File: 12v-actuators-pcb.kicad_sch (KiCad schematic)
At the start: 11 parts, among them J1 12V IN, J2 12V OUT, J3 12V OUT, J4 12V OUT, Q1 SUM110P06-08L, U1 NUCLEO-F042K6, X1 ESC_Emax_Bullet_15A, X2 ESC_Emax_Bullet_15A, X3 ESC_Emax_Bullet_15A, X4 ESC_Emax_Bullet_35A, X5 ESC_Emax_Bullet_35A

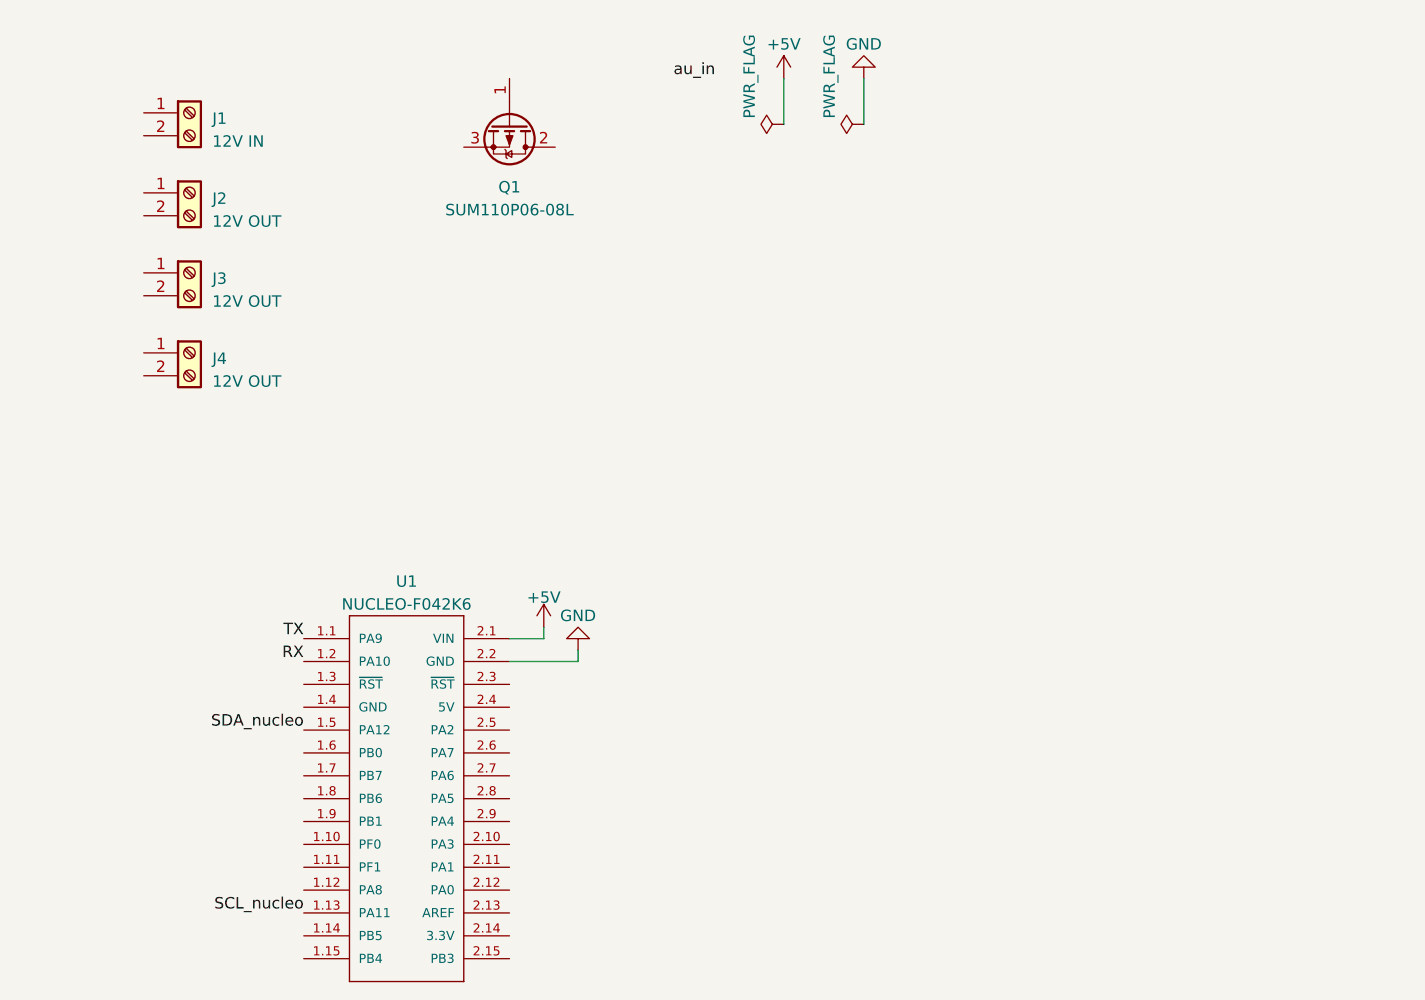
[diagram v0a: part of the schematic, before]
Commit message: WIP: Arrêt d'urgence
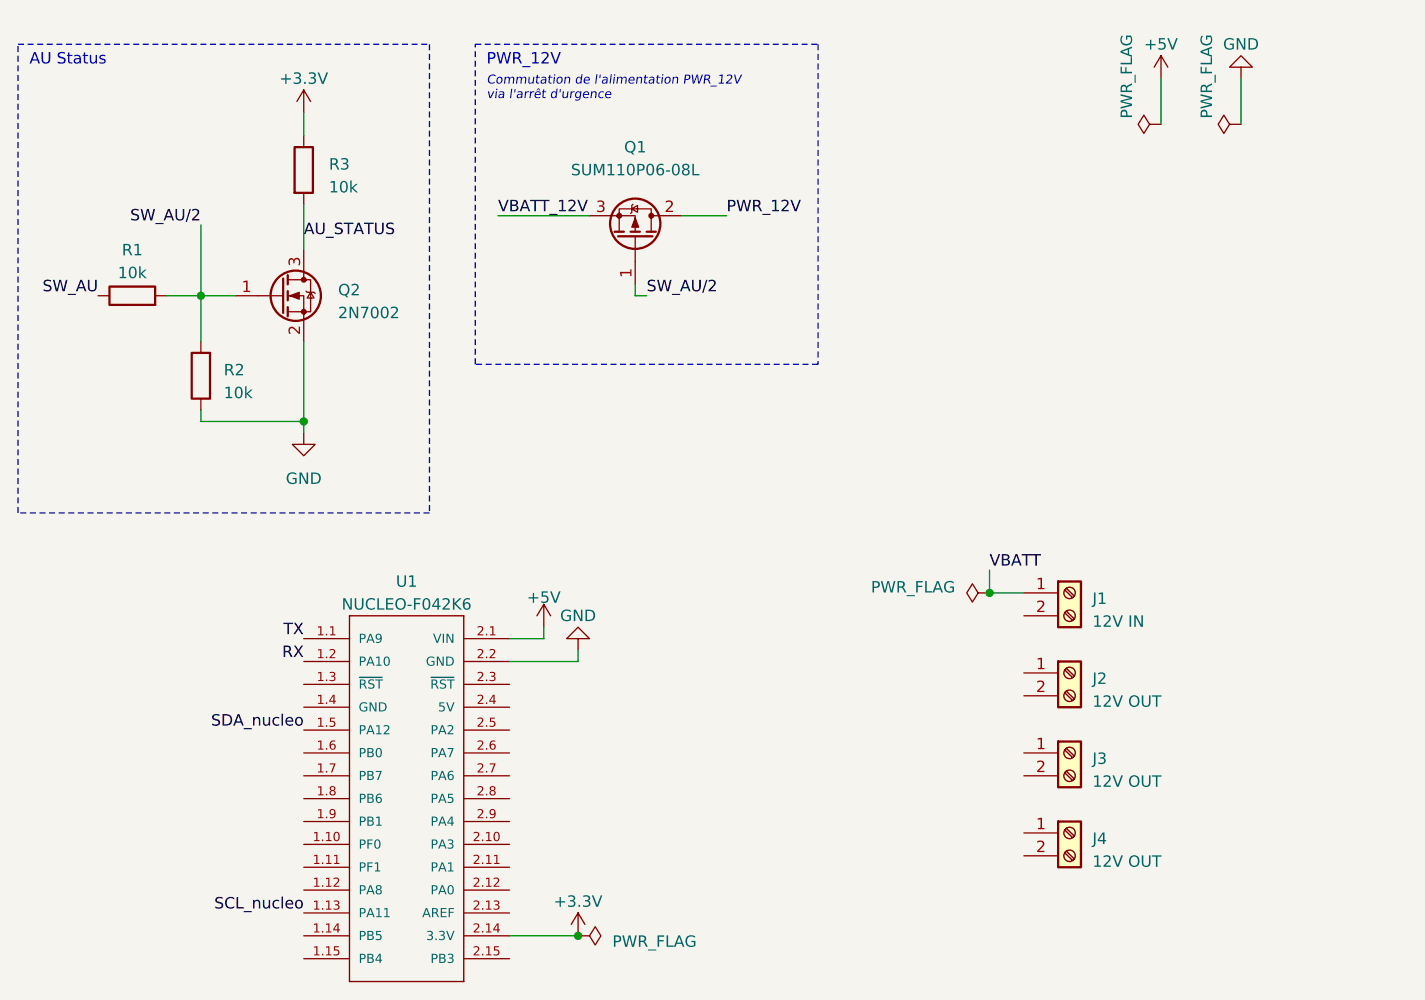
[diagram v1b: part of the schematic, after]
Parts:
- added Q2: 2N7002, Package_TO_SOT_SMD:SOT-23, symbol Transistor_FET:2N7002
- added R1, R2, R3: 10k, Resistor_SMD:R_0201_0603Metric, symbol Device:R
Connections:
- net GND: now also Q2.2 (S), R2.1
- net SW_AU/2: now reaches Q1.1 (G)
- net SW_AU/2: now also Q2.1 (G), R1.2, R2.2
- net PWR_12V: now reaches Q1.2 (D)
- net VBATT_12V: now reaches Q1.3 (S)
- net VBATT: now reaches J1.1 (Pin_1)
- net +3.3V: now reaches U1.2.14 (3.3V)
- net +3.3V: now also R3.1
- new net AU_STATUS: Q2.3 (D), R3.2
- new net SW_AU: R1.1
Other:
- note added: "AU Status"
- note added: "Commutation de l'alimentation PWR_12V via l'arrêt d'urgence"
- note added: "PWR_12V"
- moved on the sheet: J1, J2, J3, J4, Q1

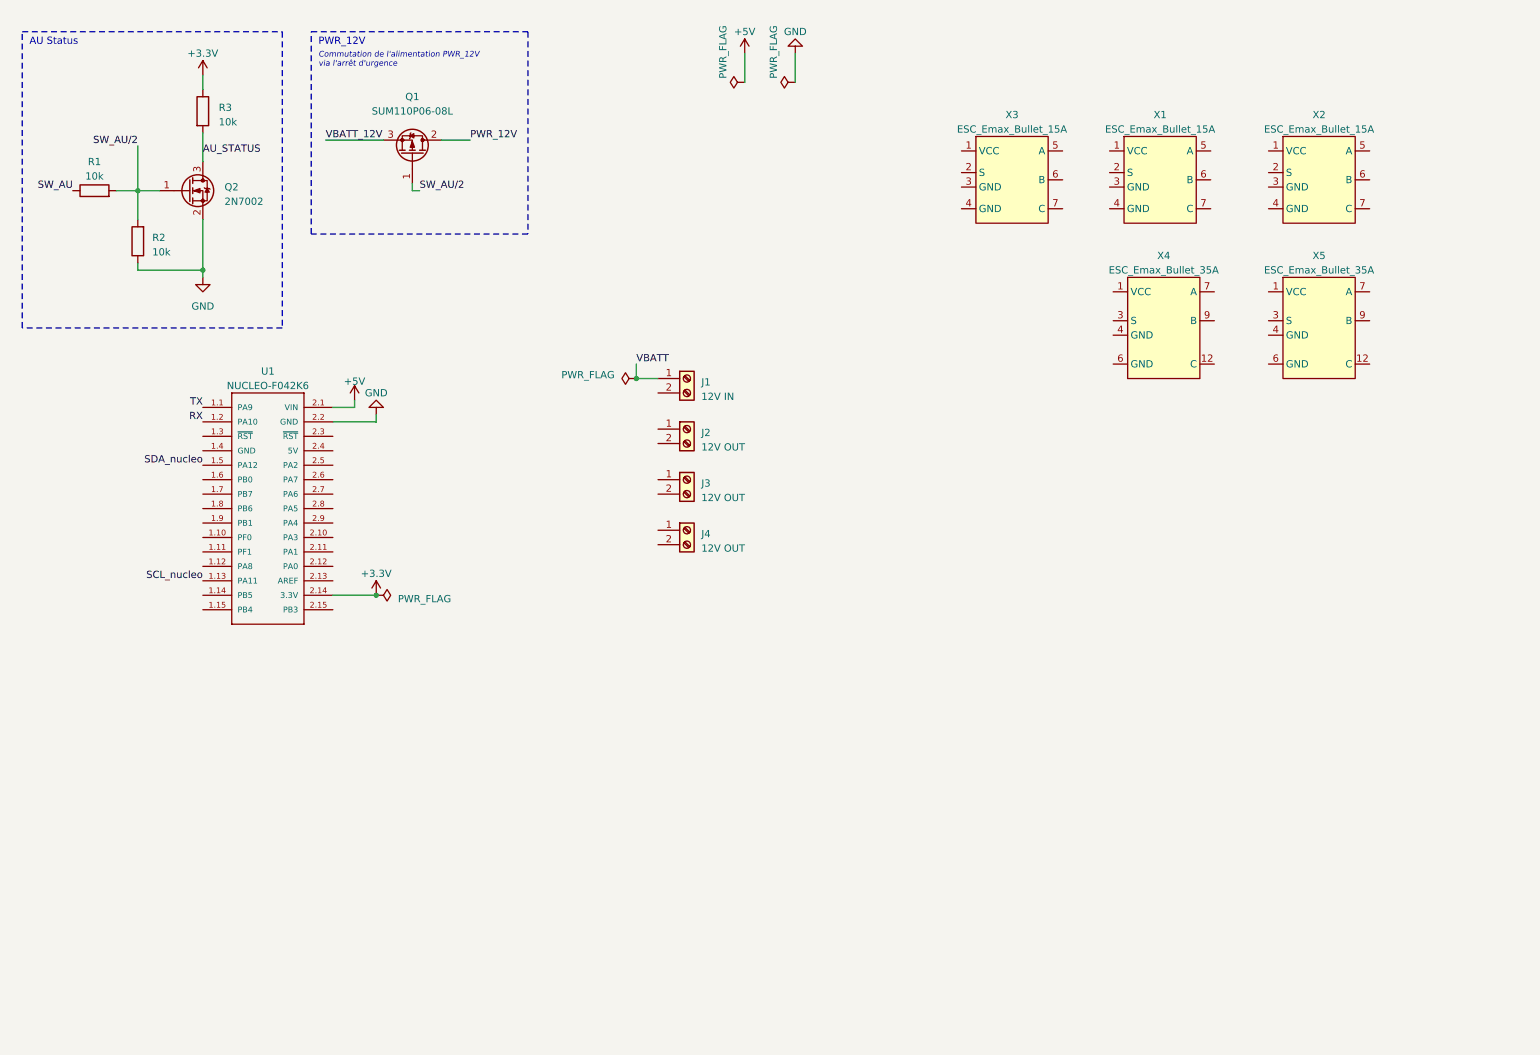
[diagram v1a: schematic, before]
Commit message: Schéma AU fait + ESC + électrovannes débuté
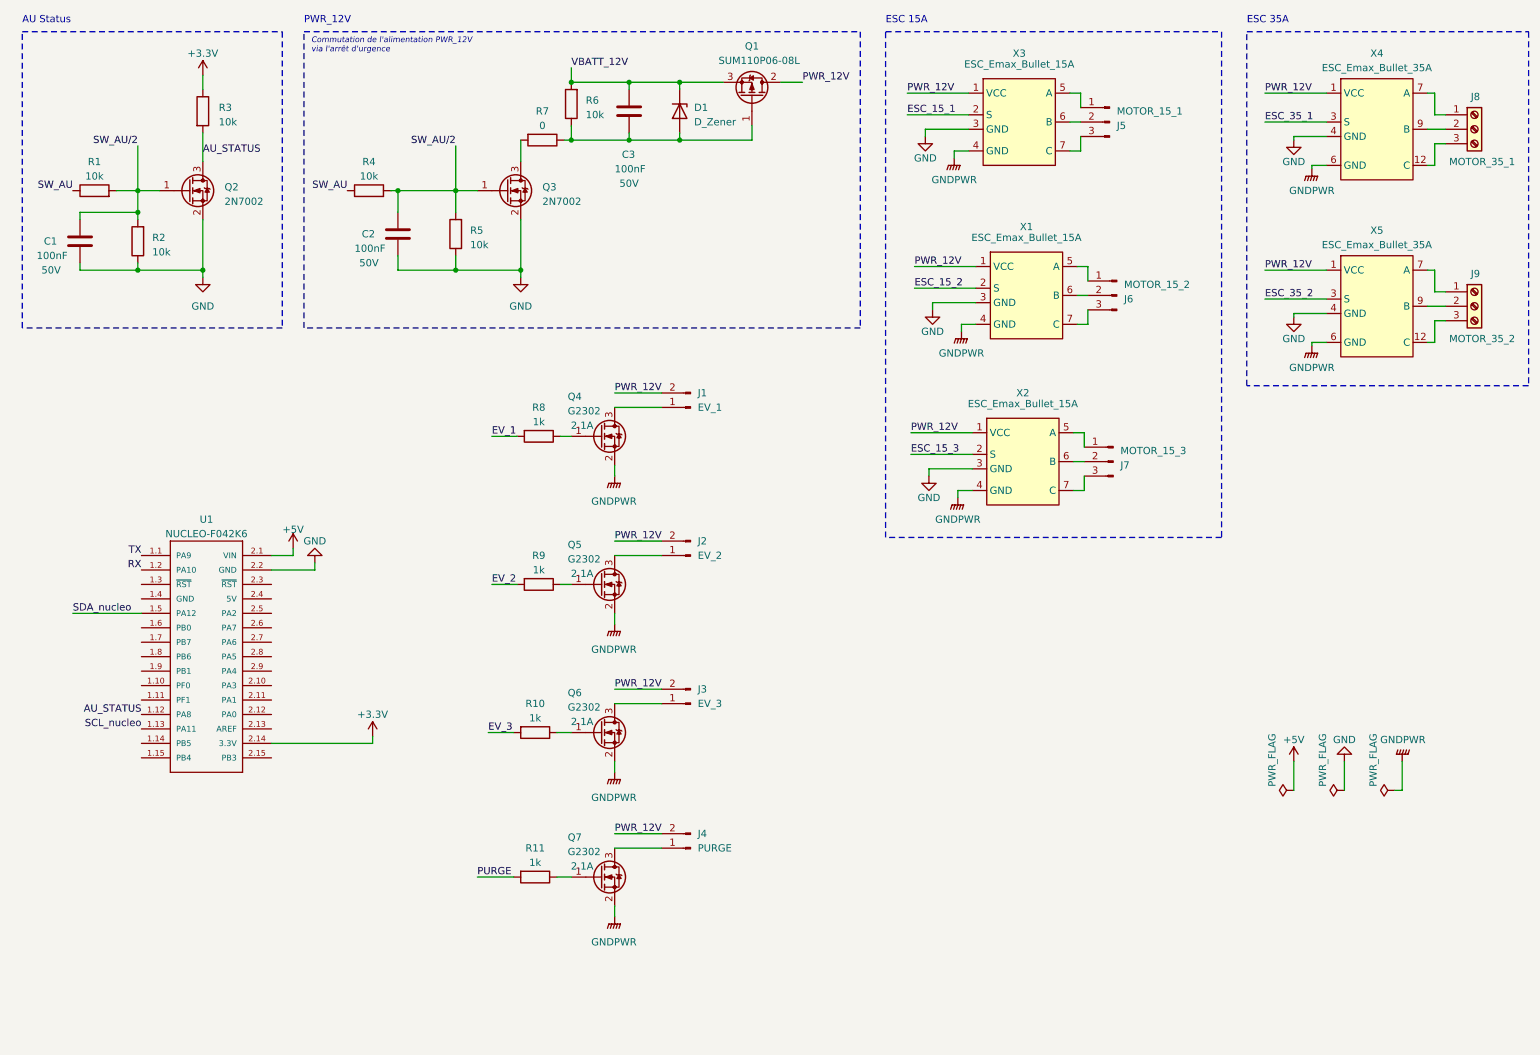
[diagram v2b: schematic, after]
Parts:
- removed J1: 12V IN, symbol Connector:Screw_Terminal_01x02
- removed J2, J3, J4: 12V OUT, symbol Connector:Screw_Terminal_01x02
- added C1, C2, C3: 100nF, symbol Device:C
- added D1: D_Zener, symbol Device:D_Zener
- added J1: EV_1, symbol Connector:Conn_01x02_Pin
- added J2: EV_2, symbol Connector:Conn_01x02_Pin
- added J3: EV_3, symbol Connector:Conn_01x02_Pin
- added J4: PURGE, symbol Connector:Conn_01x02_Pin
- added J5: MOTOR_15_1, symbol Connector:Conn_01x03_Pin
- added J6: MOTOR_15_2, symbol Connector:Conn_01x03_Pin
- added J7: MOTOR_15_3, symbol Connector:Conn_01x03_Pin
- added J8: MOTOR_35_1, symbol Connector:Screw_Terminal_01x03
- added J9: MOTOR_35_2, symbol Connector:Screw_Terminal_01x03
- added Q3: 2N7002, Package_TO_SOT_SMD:SOT-23, symbol Transistor_FET:2N7002
- added Q4, Q5, Q6, Q7: G2302, symbol Device:Q_NMOS_GSD
- added R10, R11, R8, R9: 1k, symbol Device:R
- added R4, R5, R6: 10k, Resistor_SMD:R_0201_0603Metric, symbol Device:R
- added R7: 0, Resistor_SMD:R_0201_0603Metric, symbol Device:R
- Q1: footprint Package_TO_SOT_SMD:TO-263-2 -> Package_TO_SOT_SMD:TO-252-2
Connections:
- net PWR_12V is gone; now on net VCC: Q1.2 (D)
- net AU_STATUS: now also U1.1.12 (PA8)
- net GND: now also X1.3 (GND), X1.4 (GND), X2.3 (GND), X2.4 (GND), X3.3 (GND), X3.4 (GND), X4.4 (GND), X4.6 (GND), X5.4 (GND), X5.6 (GND), C1.2, C2.2, Q3.2 (S), Q4.2 (S), Q5.2 (S), Q6.2 (S), Q7.2 (S), R5.1
- net SW_AU: now also R4.1
- net SW_AU/2: now also C1.1, C2.1, Q3.1 (G), R4.2, R5.2; no longer Q1.1 (G)
- net VBATT_12V: now also C3.1, D1.1 (K), R6.2
- net VCC: now also X1.1 (VCC), X2.1 (VCC), X3.1 (VCC), X4.1 (VCC), X5.1 (VCC), J1.2 (Pin_2), J2.2 (Pin_2), J3.2 (Pin_2), J4.2 (Pin_2)
- net at X5.10 (B): now also X5.9 (B), J9.2 (Pin_2)
- net at X5.11 (C): now also X5.12 (C), J9.3 (Pin_3)
- net ESC_35_2: now reaches X5.3 (S)
- net at X5.7 (A): now also X5.8 (A), J9.1 (Pin_1)
- net at X4.10 (B): now also X4.9 (B), J8.2 (Pin_2)
- net at X4.11 (C): now also X4.12 (C), J8.3 (Pin_3)
- net ESC_35_1: now reaches X4.3 (S)
- net at X4.7 (A): now also X4.8 (A), J8.1 (Pin_1)
- net ESC_15_3: now reaches X2.2 (S)
- net at X2.5 (A): now also J7.1 (Pin_1)
- net at X2.6 (B): now also J7.2 (Pin_2)
- net at X2.7 (C): now also J7.3 (Pin_3)
- net ESC_15_1: now reaches X3.2 (S)
- net at X3.5 (A): now also J5.1 (Pin_1)
- net at X3.6 (B): now also J5.2 (Pin_2)
- net at X3.7 (C): now also J5.3 (Pin_3)
- net ESC_15_2: now reaches X1.2 (S)
- net at X1.5 (A): now also J6.1 (Pin_1)
- net at X1.6 (B): now also J6.2 (Pin_2)
- net at X1.7 (C): now also J6.3 (Pin_3)
- new net: Q7.1 (G), R11.1
- new net: Q6.1 (G), R10.1
- new net: J2.1 (Pin_1), Q5.3 (D)
- new net: Q3.3 (D), R7.2
- new net: C3.2, D1.2 (A), Q1.1 (G), R6.1, R7.1
- new net: Q4.1 (G), R8.1
- new net: J1.1 (Pin_1), Q4.3 (D)
- new net: J3.1 (Pin_1), Q6.3 (D)
- new net: J4.1 (Pin_1), Q7.3 (D)
- new net: Q5.1 (G), R9.1
- new net EV_1: R8.2
- new net EV_2: R9.2
- new net EV_3: R10.2
- new net PURGE: R11.2
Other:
- note added: "ESC 15A"
- note added: "ESC 35A"
- moved on the sheet: Q1, U1, X3, X4

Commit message: Schematics mostly done, EV and ESC pins to validate with @MGMaximusk
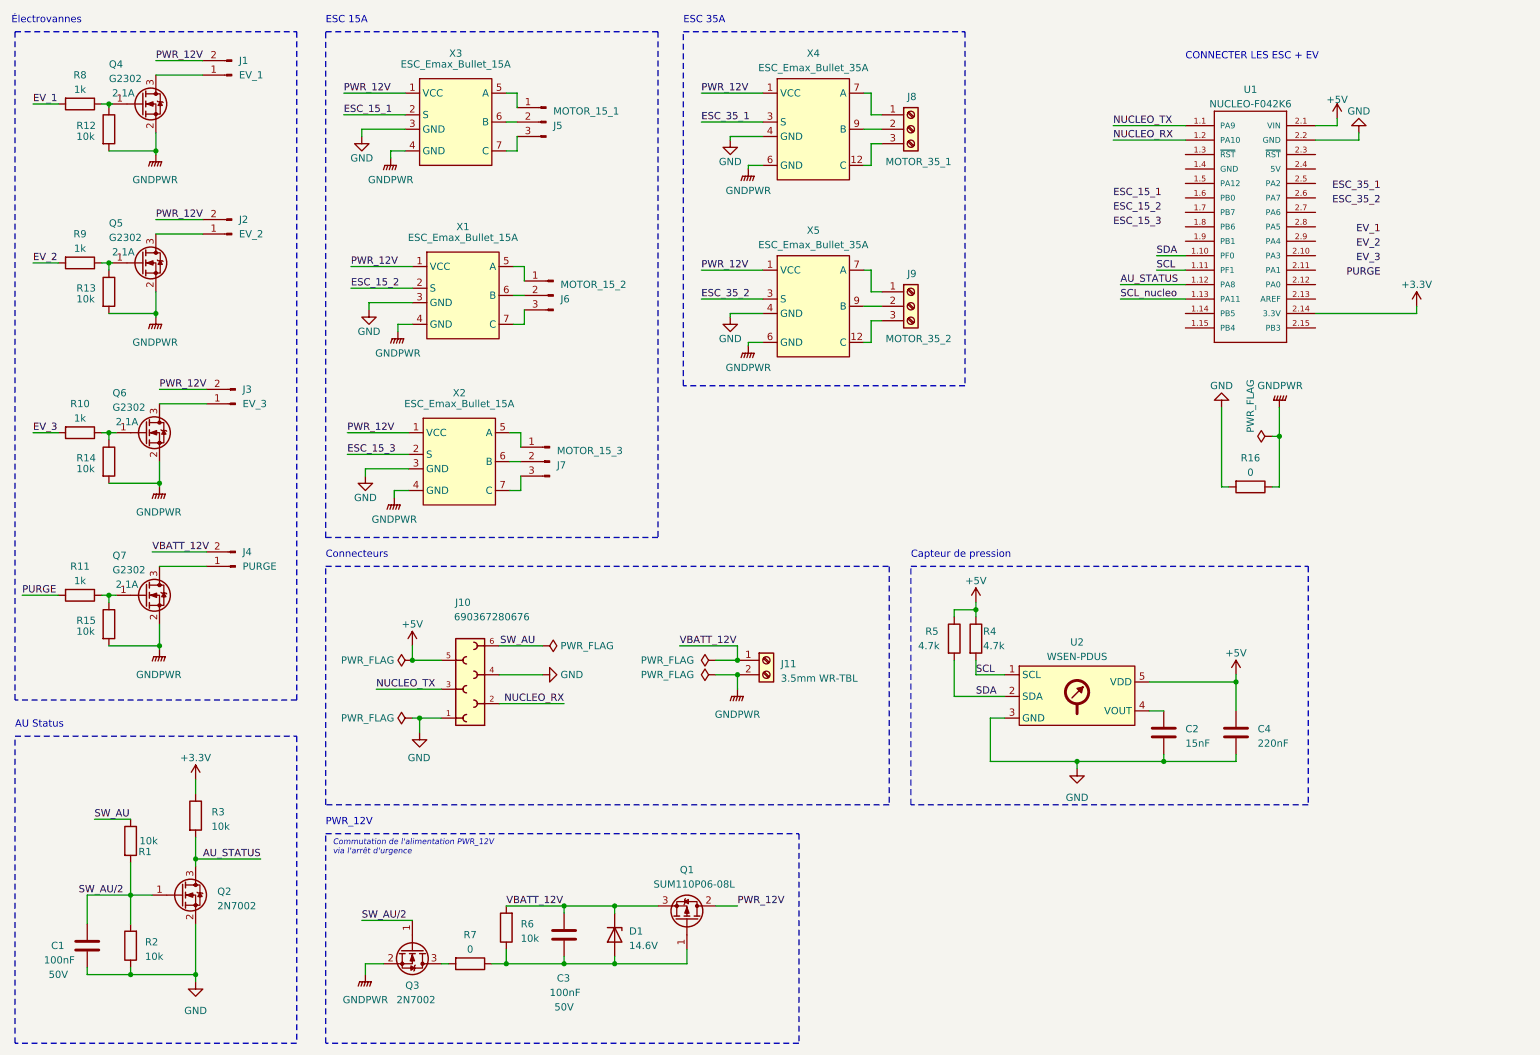
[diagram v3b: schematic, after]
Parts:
- added C4: 220nF, symbol Device:C
- added J10: 690367280676, ConnectorsEvo:690367280676, symbol ComponentsEvo:690367280676
- added J11: 3.5mm WR-TBL, symbol Connector:Screw_Terminal_01x02
- added R12, R13, R14, R15: 10k, symbol Device:R
- added R16: 0, symbol Device:R
- added U2: WSEN-PDUS, symbol ComponentsEvo:WSEN-PDUS
- C2: value 100nF -> 15nF; Max voltage 50V -> (none)
- D1: value D_Zener -> 14.6V
- R4, R5: value 10k -> 4.7k; footprint Resistor_SMD:R_0201_0603Metric -> (none)
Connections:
- net +5V: now also R4.1, R5.1, C4.1, J10.5, U2.5 (VDD)
- net GND: now also C4.2, J10.1, J10.4, J11.2 (Pin_2), R12.2, R13.2, R14.2, R15.2, R16.1, R16.2, U2.3 (GND); no longer R5.1
- net SW_AU: now also J10.6; no longer R4.1
- net SW_AU/2: no longer C2.1, R4.2, R5.2
- net VBATT_12V: now also J4.2 (Pin_2), J11.1 (Pin_1)
- net VCC: no longer J4.2 (Pin_2)
- net at Q7.1 (G), R11.1: now also R15.1
- net at Q6.1 (G), R10.1: now also R14.1
- net at Q4.1 (G), R8.1: now also R12.1
- net at Q5.1 (G), R9.1: now also R13.1
- net SDA: now reaches U1.1.10 (PF0)
- net SDA: now also R5.2, U2.2 (SDA)
- net SCL: now reaches U1.1.11 (PF1)
- net SCL: now also R4.2, U2.1 (SCL)
- net RX renamed NUCLEO_RX
- net NUCLEO_RX: now also J10.2
- net SDA_nucleo: no longer names the net of U1.1.5 (PA12)
- net TX renamed NUCLEO_TX
- net NUCLEO_TX: now also J10.3
- new net: C2.1, U2.4 (VOUT)
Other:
- note added: "CONNECTER LES ESC + EV"
- note added: "Capteur de pression"
- note added: "Connecteurs"
- note added: "Électrovannes"
- moved on the sheet: C1, C3, D1, J1, J2, J3, J4, J5, J6, J7, J8, J9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

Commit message: Ajout du logo de l'équipe
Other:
- company: (none) -> Équipe Goldorak
- title: (none) -> Carte pneumatique
